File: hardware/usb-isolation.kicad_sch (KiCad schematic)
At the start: 7 parts, among them IC1 NCV1117ST33T3G, J1 USB_C_Receptacle_USB2.0_16P

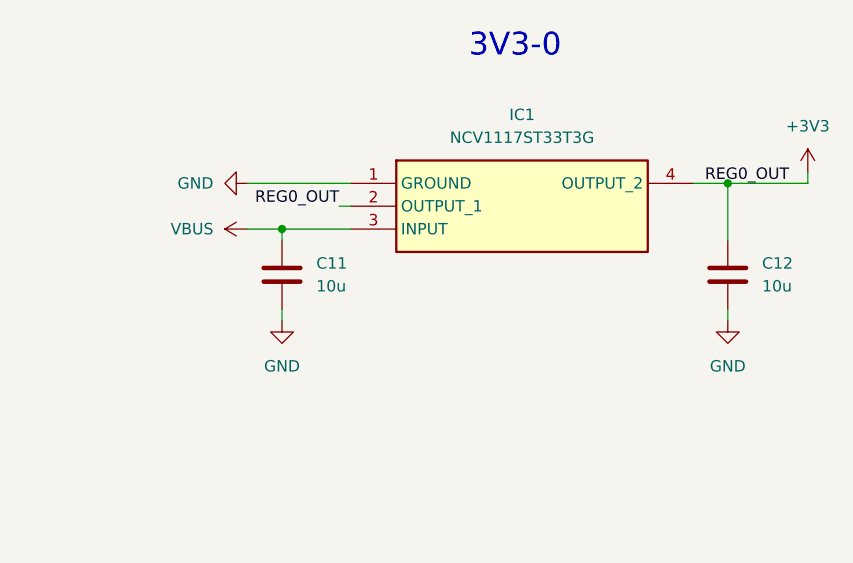
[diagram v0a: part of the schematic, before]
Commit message: Moved GND points, revised DCDC and base USB Work
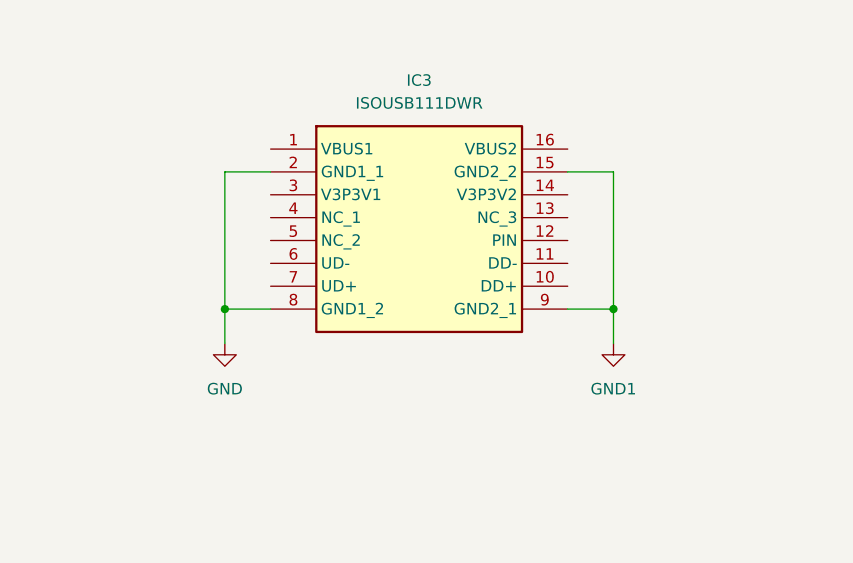
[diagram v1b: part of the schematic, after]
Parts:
- removed C11, C12: 10u, Capacitor_SMD:C_0805_2012Metric, symbol Device:C
- removed IC1: NCV1117ST33T3G, Stuttgart:SOT230P700X180-4N, symbol Stuttgart:NCV1117ST33T3G
- added IC3: ISOUSB111DWR, Stuttgart:SOIC127P1030X265-16N, symbol Stuttgart:ISOUSB111DWR
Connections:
- net GND: now also IC3.2 (GND1_1), IC3.8 (GND1_2)
- new net GND1: IC3.15 (GND2_2), IC3.9 (GND2_1)
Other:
- note removed: "3V3-0"

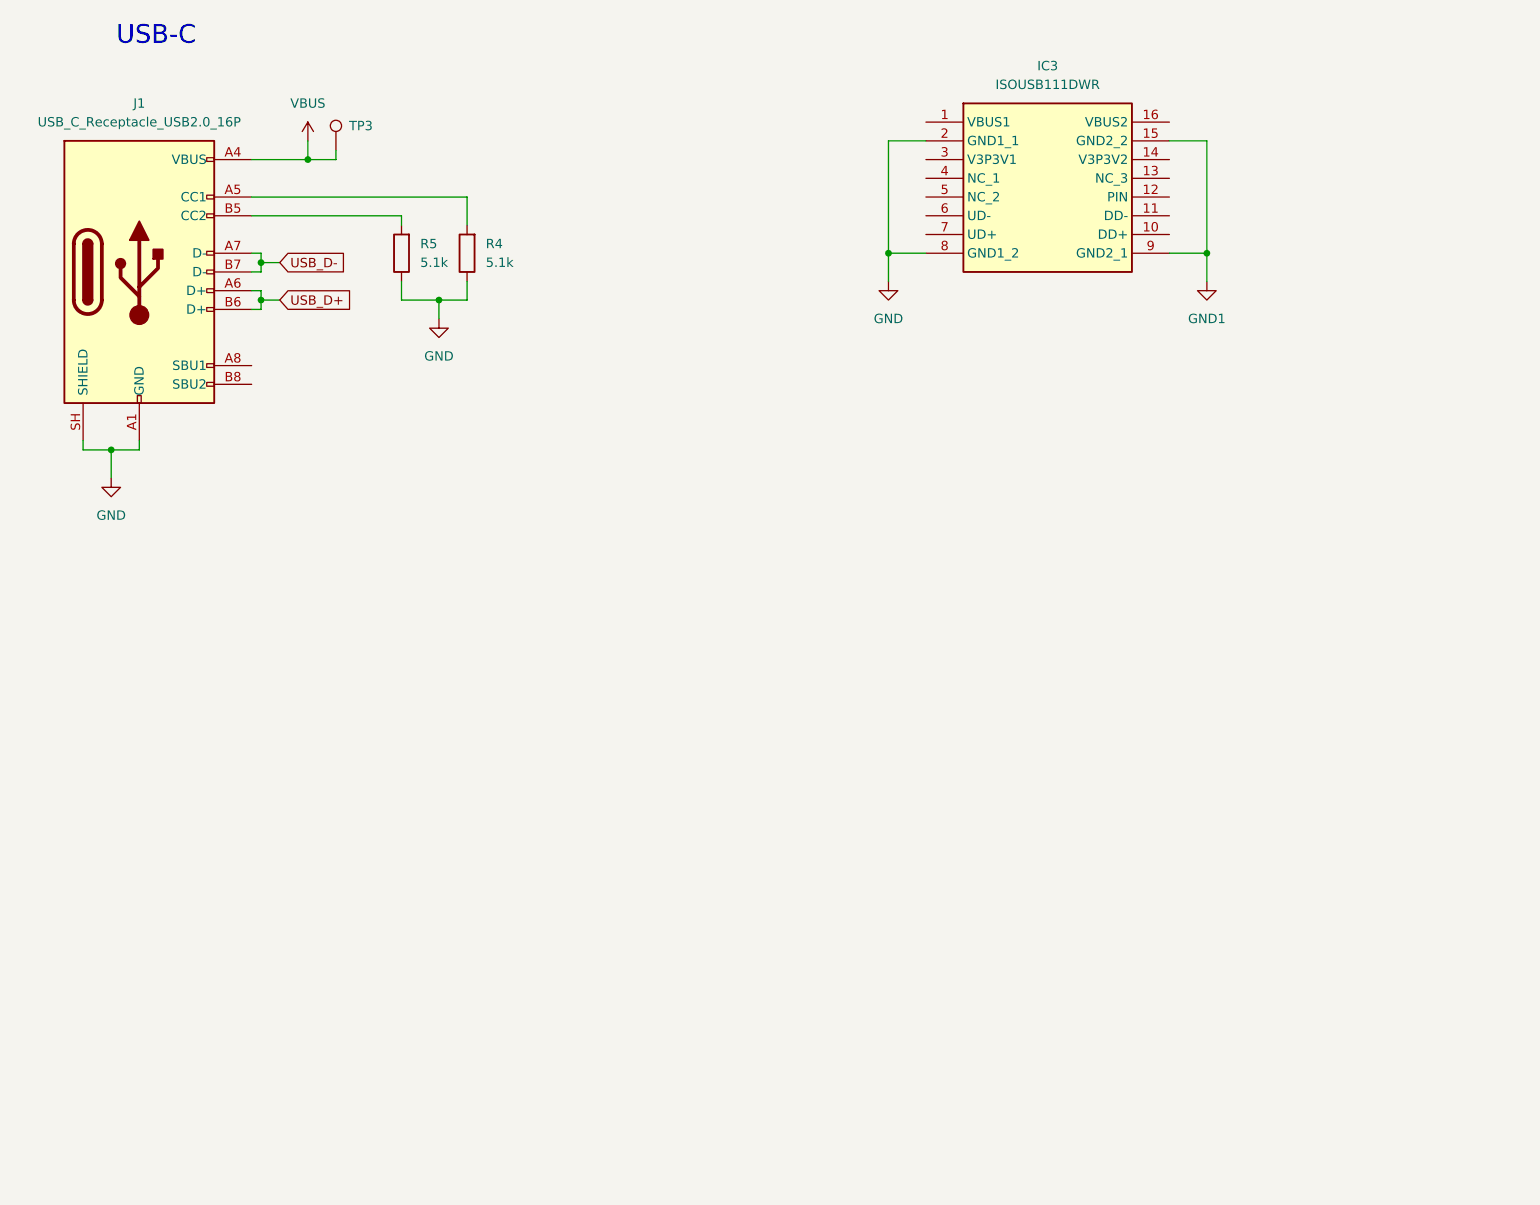
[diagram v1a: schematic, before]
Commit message: Improved USB Protection
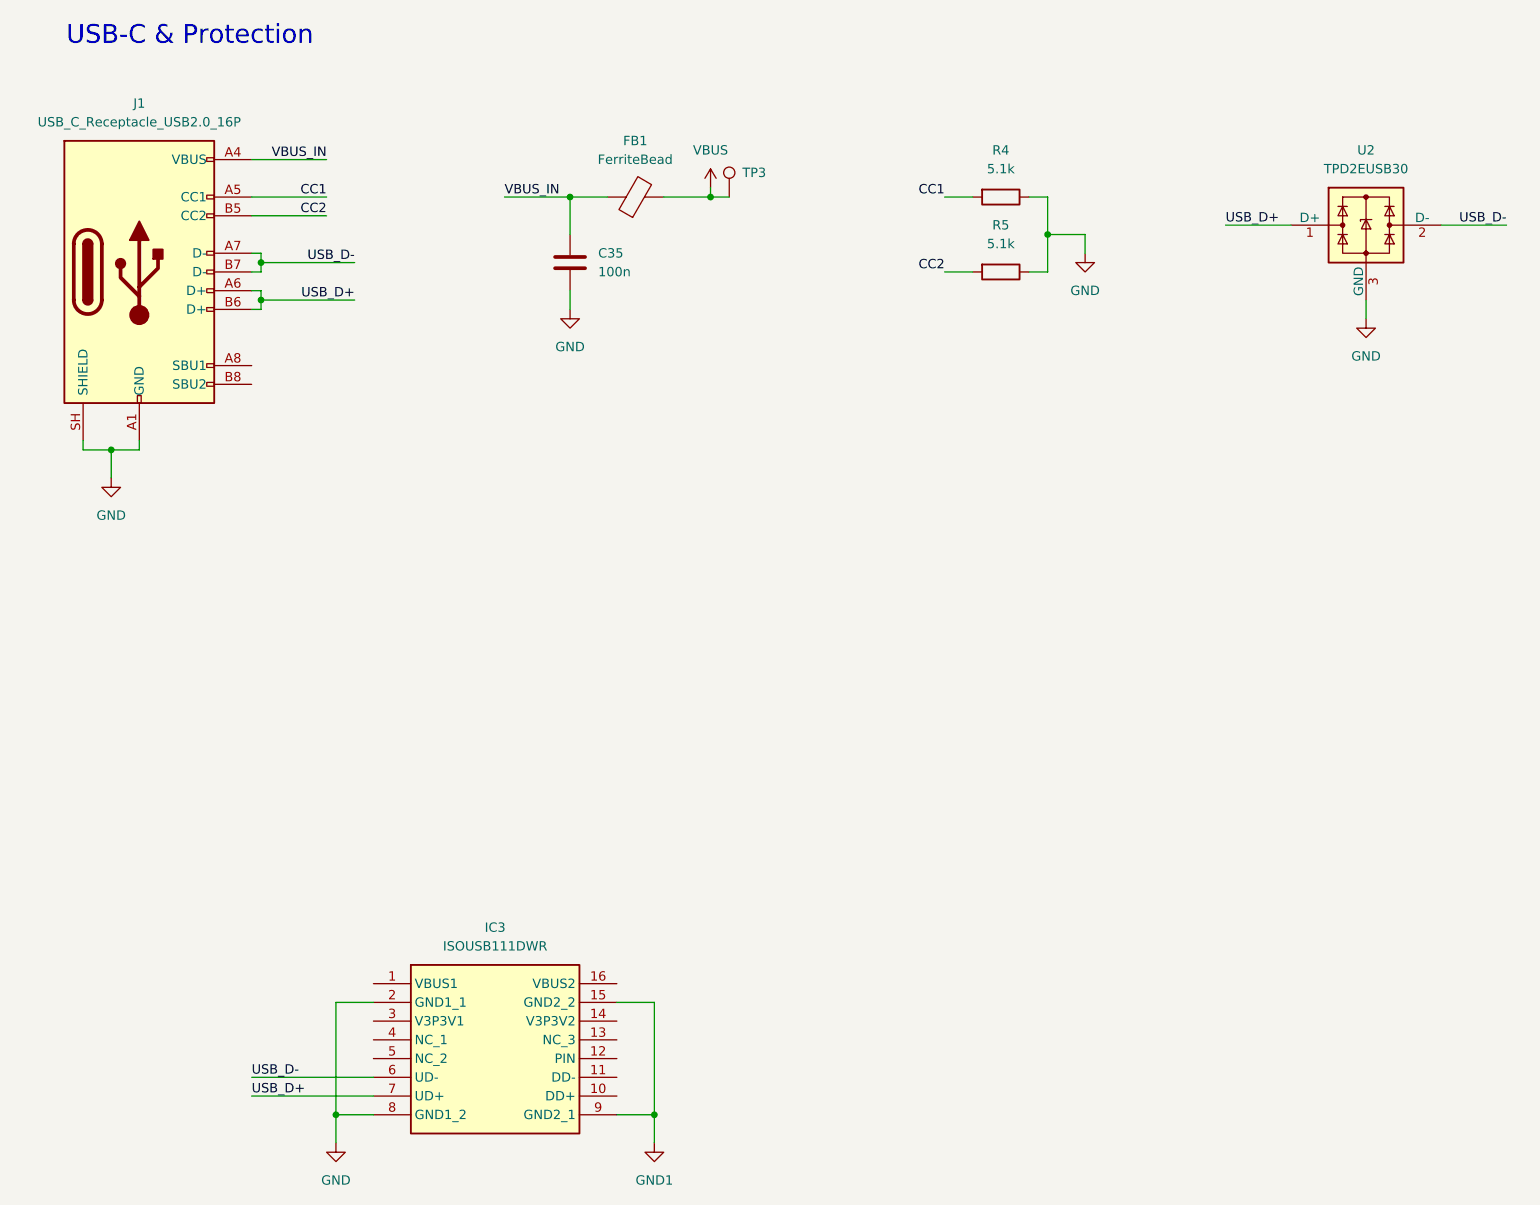
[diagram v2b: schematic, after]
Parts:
- added C35: 100n, Capacitor_SMD:C_0603_1608Metric, symbol Device:C
- added FB1: FerriteBead, Inductor_SMD:L_0603_1608Metric, symbol Device:FerriteBead
- added U2: TPD2EUSB30, Package_TO_SOT_SMD:Texas_DRT-3, symbol Power_Protection:TPD2EUSB30
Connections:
- net GND: now also C35.2, U2.3 (GND)
- net USB_D+: now also IC3.7 (UD+), U2.1 (D+)
- net USB_D-: now also IC3.6 (UD-), U2.2 (D-)
- net VBUS: now also FB1.2; no longer J1.A4 (VBUS), J1.A9 (VBUS), J1.B4 (VBUS), J1.B9 (VBUS)
- net CC1: now reaches J1.A5 (CC1), R4.2
- net CC2: now reaches J1.B5 (CC2), R5.2
- new net VBUS_IN: C35.1, FB1.1, J1.A4 (VBUS), J1.A9 (VBUS), J1.B4 (VBUS), J1.B9 (VBUS)
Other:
- note added: "USB-C & Protection"
- note removed: "USB-C"
- moved on the sheet: IC3, R4, R5, TP3

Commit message: Schematic complete and base components placed
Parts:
- added C36, C37: 1u, Capacitor_SMD:C_0603_1608Metric, symbol Device:C
- added C38, C39: 0.1u, Capacitor_SMD:C_0603_1608Metric, symbol Device:C
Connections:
- net GND: now also C36.2, C38.2
- net GND1: now also C37.2, C39.2
- net USB_D+: now also IC3.10 (DD+)
- net USB_D-: now also IC3.11 (DD-)
- net VBUS: now also IC3.1 (VBUS1), C36.1
- net at IC3.12 (PIN): now also IC3.14 (V3P3V2), C39.1
- net +5V: now reaches IC3.16 (VBUS2)
- net +5V: now also C37.1
- net at IC3.3 (V3P3V1): now also C38.1
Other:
- note added: "USB Isolation"
- moved on the sheet: IC3

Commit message: Hardware layout complete
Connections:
- net USB_D+: no longer IC3.7 (UD+), J1.A6 (D+), J1.B6 (D+), U2.1 (D+)
- net USB_D-: no longer IC3.6 (UD-), J1.A7 (D-), J1.B7 (D-), U2.2 (D-)
- new net USB_C_D+: IC3.7 (UD+), J1.A6 (D+), J1.B6 (D+), U2.1 (D+)
- new net USB_C_D-: IC3.6 (UD-), J1.A7 (D-), J1.B7 (D-), U2.2 (D-)
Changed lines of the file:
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@@
 	(wire
 		(pts
-			(xy 69.85 139.7) (xy 80.01 139.7)
+			(xy 68.58 139.7) (xy 80.01 139.7)
 		)
 		(stroke
@@
 	(wire
 		(pts
-			(xy 226.06 53.34) (xy 234.95 53.34)
+			(xy 226.06 53.34) (xy 237.49 53.34)
 		)
 		(stroke
@@
 	(wire
 		(pts
-			(xy 69.85 142.24) (xy 80.01 142.24)
-		)
-		(stroke
-			(width 0)
-			(type default)
-		)
-	)
-	(wire
-		(pts
-			(xy 196.85 53.34) (xy 205.74 53.34)
+			(xy 68.58 142.24) (xy 80.01 142.24)
+		)
+		(stroke
+			(width 0)
+			(type default)
+		)
+	)
+	(wire
+		(pts
+			(xy 194.31 53.34) (xy 205.74 53.34)
 		)
 		(stroke
@@
 		)
 	)
-	(label "USB_D-"
-		(at 69.85 139.7 0)
+	(label "USB_C_D-"
+		(at 68.58 139.7 0)
 		(effects
 			(font
@@
 		)
 	)
-	(label "USB_D-"
-		(at 234.95 53.34 180)
-		(effects
-			(font
-				(size 1.27 1.27)
-			)
-			(justify right bottom)
-		)
-	)
-	(label "USB_D+"
-		(at 69.85 142.24 0)
+	(label "USB_C_D-"
+		(at 237.49 53.34 180)
+		(effects
+			(font
+				(size 1.27 1.27)
+			)
+			(justify right bottom)
+		)
+	)
+	(label "USB_C_D+"
+		(at 68.58 142.24 0)
 		(effects
 			(font
@@
 		)
 	)
-	(label "USB_D-"
+	(label "USB_C_D-"
 		(at 78.74 58.42 180)
 		(effects
@@
 		)
 	)
-	(label "USB_D+"
+	(label "USB_C_D+"
 		(at 78.74 63.5 180)
 		(effects
@@
 		)
 	)
-	(label "USB_D+"
-		(at 196.85 53.34 0)
-		(effects
-			(font
+	(label "USB_C_D+"
+		(at 194.31 53.34 0)
+		(effects
+			(font

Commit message: Schematic Clean Up
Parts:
- FB1: JLC Part Number (none) -> C82155
- IC3: JLC Part Number (none) -> C5216549
- J1: JLC Part Number (none) -> C3025063
- TP3: now left out of the parts list
- U2: JLC Part Number (none) -> C97502
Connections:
- no-connect marks 0 -> 5
